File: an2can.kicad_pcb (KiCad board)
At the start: 2 copper layers, 76.7 x 51.9 mm, 130 parts, among them J1 PWR/CAN, J2 USB C, J3 DBG, J4 5V IN, J5 Input, J6 Aux, J7 Input, J8 Input, J9 Input, Q1 PMV65XP, SW1 RESET, U1 MAX6025, U10 AD8221ARZ, U11 Opamp_Dual, U12 AD8221ARZ, U13 Opamp_Dual, U2 Tex_DCDC_v2, U3 DSC61XX, U4 STM32L432KCUx, U5 MCP2562FD, U6 AD8221ARZ, U7 Opamp_Dual, U8 AD8221ARZ, U9 Opamp_Dual

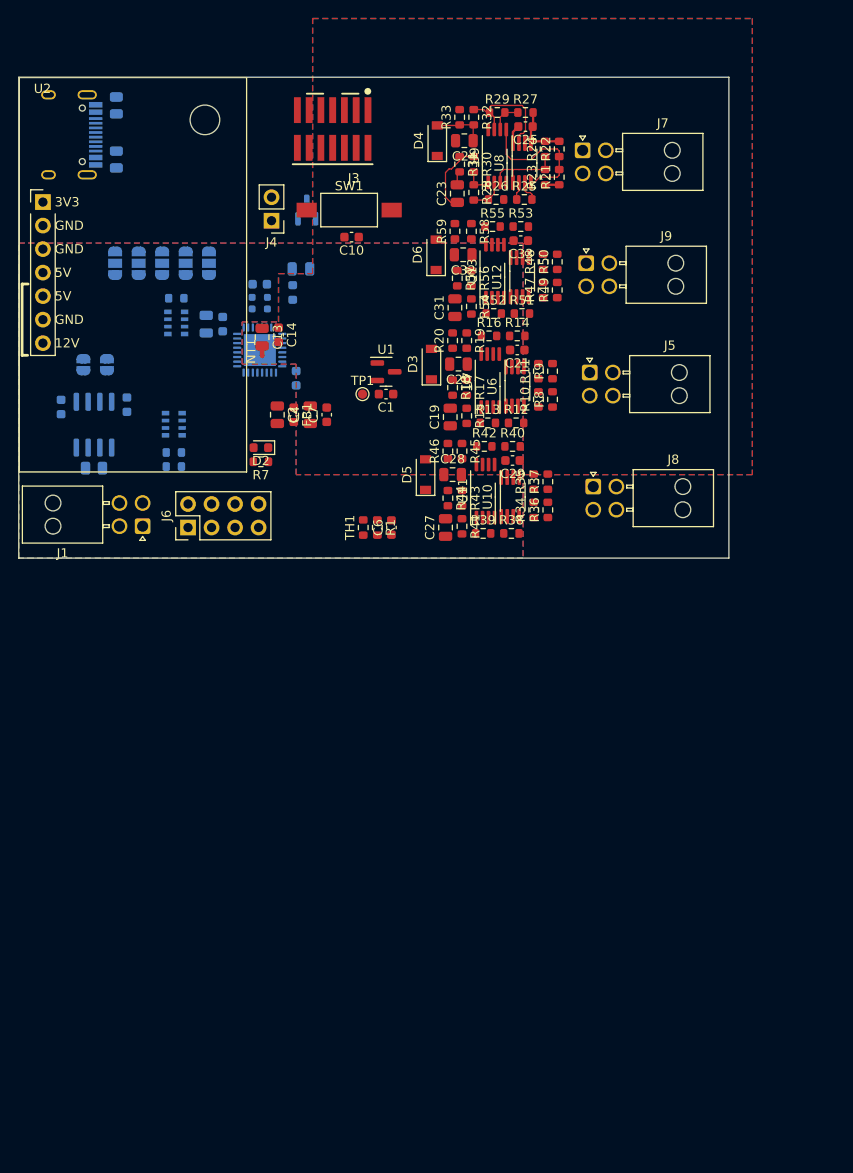
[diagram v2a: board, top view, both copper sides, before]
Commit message: pcb: define routing of input stage
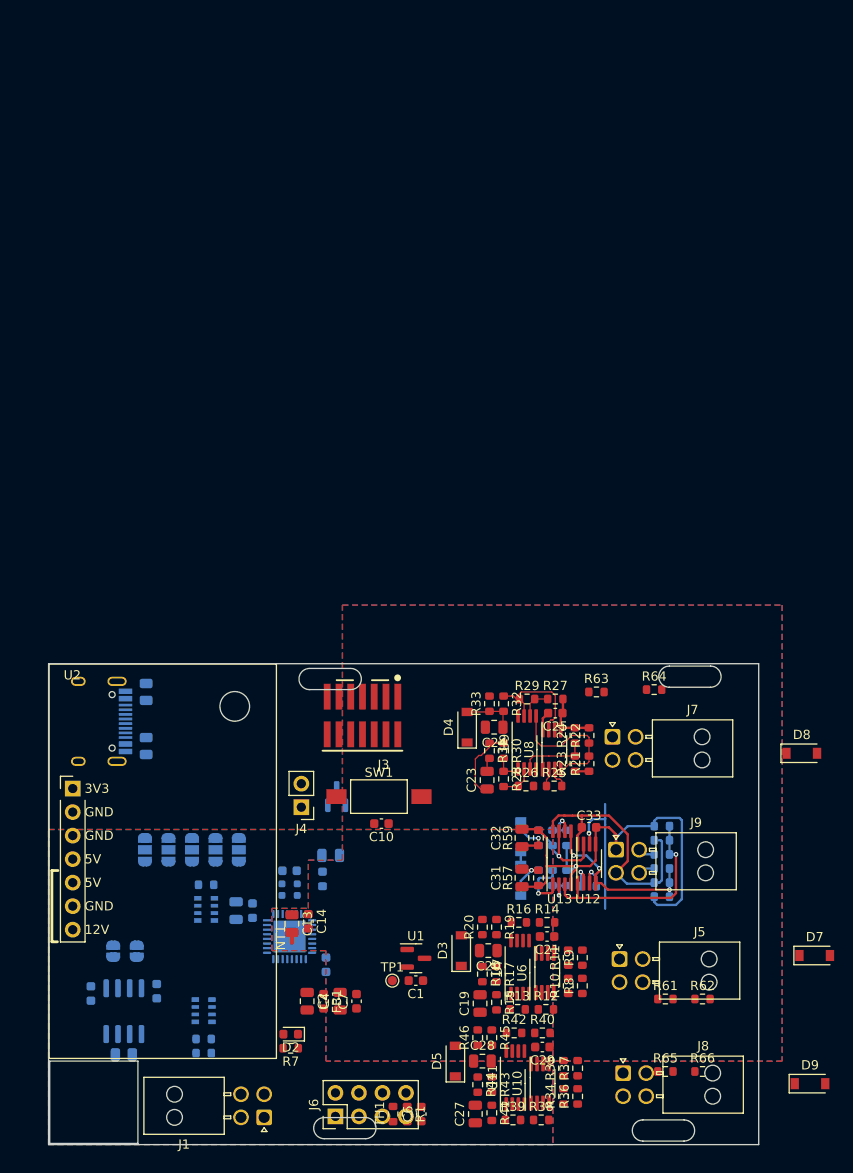
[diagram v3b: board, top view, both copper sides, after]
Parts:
- added D10: D_Schottky, Diode_SMD:D_SOD-123, B.Cu at (106.8, 88.3)
- added D7: D_Schottky, Diode_SMD:D_SOD-123, F.Cu at (138.6, 96.4)
- added D8: D_Schottky, Diode_SMD:D_SOD-123, F.Cu at (137.2, 74.5)
- added D9: D_Schottky, Diode_SMD:D_SOD-123, F.Cu at (138.0, 110.2)
- added R61: R, Resistor_SMD:R_0603_1608Metric, F.Cu at (122.4, 101.1)
- added R62: R, Resistor_SMD:R_0603_1608Metric, F.Cu at (126.4, 101.1)
- added R63: R, Resistor_SMD:R_0603_1608Metric, F.Cu at (115.0, 67.9)
- added R64: R, Resistor_SMD:R_0603_1608Metric, F.Cu at (121.2, 67.7)
- added R65: R, Resistor_SMD:R_0603_1608Metric, F.Cu at (122.4, 108.9)
- added R66: R, Resistor_SMD:R_0603_1608Metric, F.Cu at (126.4, 108.9)
- added R67: R, Resistor_SMD:R_0603_1608Metric, B.Cu at (122.0, 87.0)
- added R68: R, Resistor_SMD:R_0603_1608Metric, B.Cu at (122.0, 85.5)
- D6, R47, R48, R49, R50, R51, R52, R53, R54, R55, R56, R58: moved to B.Cu
- moved R48 69.8 mm to (122.0, 90.0), turned to 180 degrees
- moved R55 66.4 mm to (110.2, 83.7), turned to 90 degrees
- moved R53 66.2 mm to (111.8, 83.7), turned to -90 degrees
- moved R59 66.1 mm to (108.7, 83.7)
- moved R58 65.9 mm to (108.7, 83.7)
- moved J6 65.6 mm to (86.8, 113.8)
- moved R57 65.4 mm to (108.7, 88.0)
- moved R47 65.3 mm to (122.0, 88.5), turned to 0 degrees
- moved J1 65.2 mm to (79.1, 113.9)
- moved R56 65.2 mm to (108.7, 88.0)
- moved C33 63.8 mm to (114.2, 82.5)
- moved U12 63.8 mm to (113.9, 86.5)
- moved U13 63.8 mm to (111.3, 85.8)
- moved D6 63.5 mm to (106.8, 83.6)
- moved FB2 63.4 mm to (85.4, 88.1)
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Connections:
- J5 pad 1: /Input Stage 2/IN_0+ -> GNDA
- J5 pad 2: /Input Stage 2/IN_1+ -> +5VA
- J5 pad 3: +5VA -> /Input Stage 2/IN_1
- J5 pad 4: GNDA -> /Input Stage 2/IN_0
- J7 pad 1: /Input Stage 1/IN_0+ -> GNDA
- J7 pad 2: /Input Stage 1/IN_1+ -> +5VA
- J7 pad 3: +5VA -> /Input Stage 1/IN_1
- J7 pad 4: GNDA -> /Input Stage 1/IN_0
- J8 pad 1: /Input Stage 3/IN_0+ -> GNDA
- J8 pad 2: /Input Stage 3/IN_1+ -> +5VA
- J8 pad 3: +5VA -> /Input Stage 3/IN_1
- J8 pad 4: GNDA -> /Input Stage 3/IN_0
- J9 pad 1: /Input Stage 4/IN_0+ -> GNDA
- J9 pad 2: /Input Stage 4/IN_1+ -> +5VA
- J9 pad 3: +5VA -> /Input Stage 4/IN_1
- J9 pad 4: GNDA -> /Input Stage 4/IN_0
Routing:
- net GNDA: track 7.89 -> 60.0 mm, vias 0 -> 1
- net +5VA: track 3.59 -> 32.4 mm
- net /Input Stage 4/IN_1+: track 0.00 -> 23.0 mm, vias 0 -> 1
- net /Input Stage 4/IN_0+: track 0.00 -> 19.2 mm, vias 0 -> 3
- net /2V5_OFFSET: track 0.00 -> 15.6 mm, vias 0 -> 1
- net /Input Stage 4/OUT_COM_UNFLT: track 0.00 -> 10.8 mm, vias 0 -> 1
- net /Input Stage 4/OUT_COM: track 0.00 -> 6.60 mm, vias 0 -> 1
- net /Input Stage 4/OUT_SINGLE_UNFLT: track 0.00 -> 6.32 mm, vias 0 -> 1
- net /Input Stage 4/OUT_SINGLE: track 0.00 -> 5.79 mm, vias 0 -> 1
- net /Input Stage 4/IN_1-: track 0.00 -> 4.43 mm, vias 0 -> 1
- net /Input Stage 4/IN_0-: track 0.00 -> 3.84 mm, vias 0 -> 1
- net /Input Stage 4/RG2: track 0.00 -> 3.04 mm, vias 0 -> 1
- net /Input Stage 4/RG1: track 0.00 -> 2.88 mm, vias 0 -> 1
- net /Input Stage 4/IN_1: track 0.00 -> 1.84 mm
- net /Input Stage 4/IN_0: track 0.00 -> 1.82 mm
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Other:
- outline, holes or cut-outs redrawn

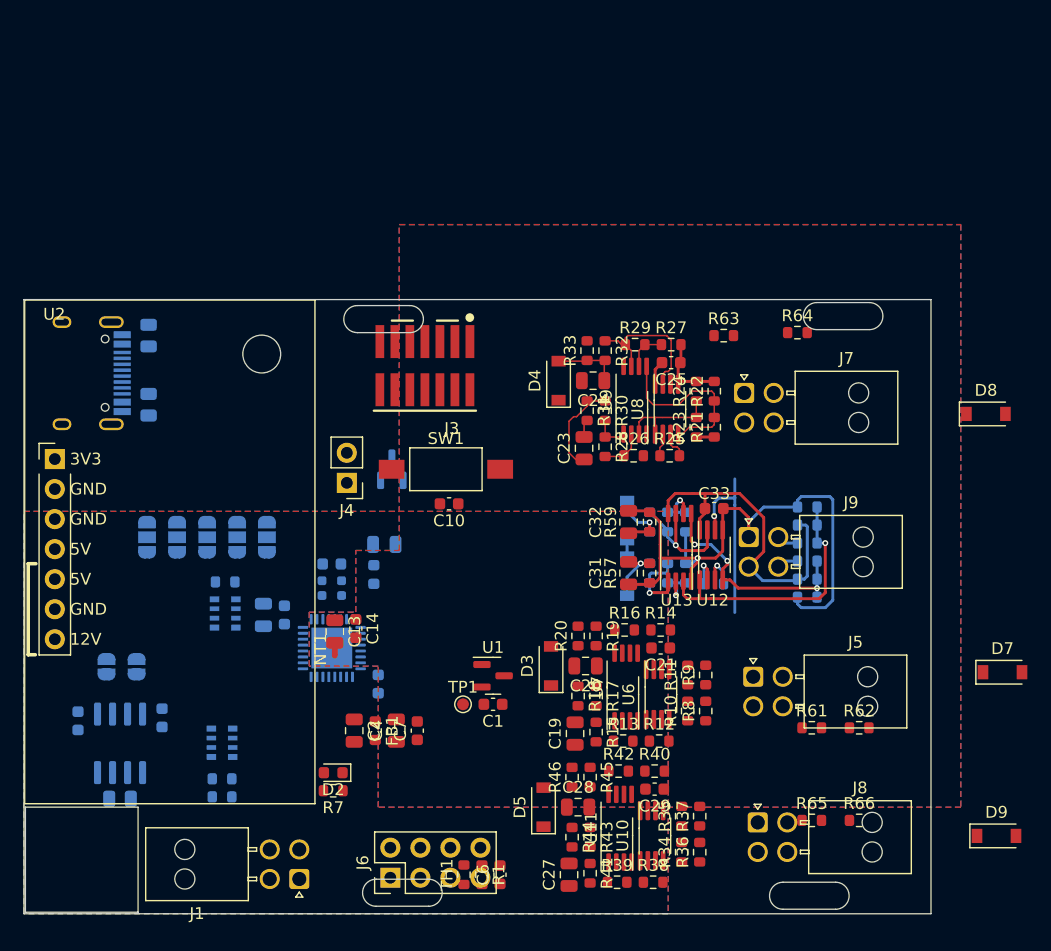
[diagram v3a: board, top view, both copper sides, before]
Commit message: pcb: finalize routing of analog section
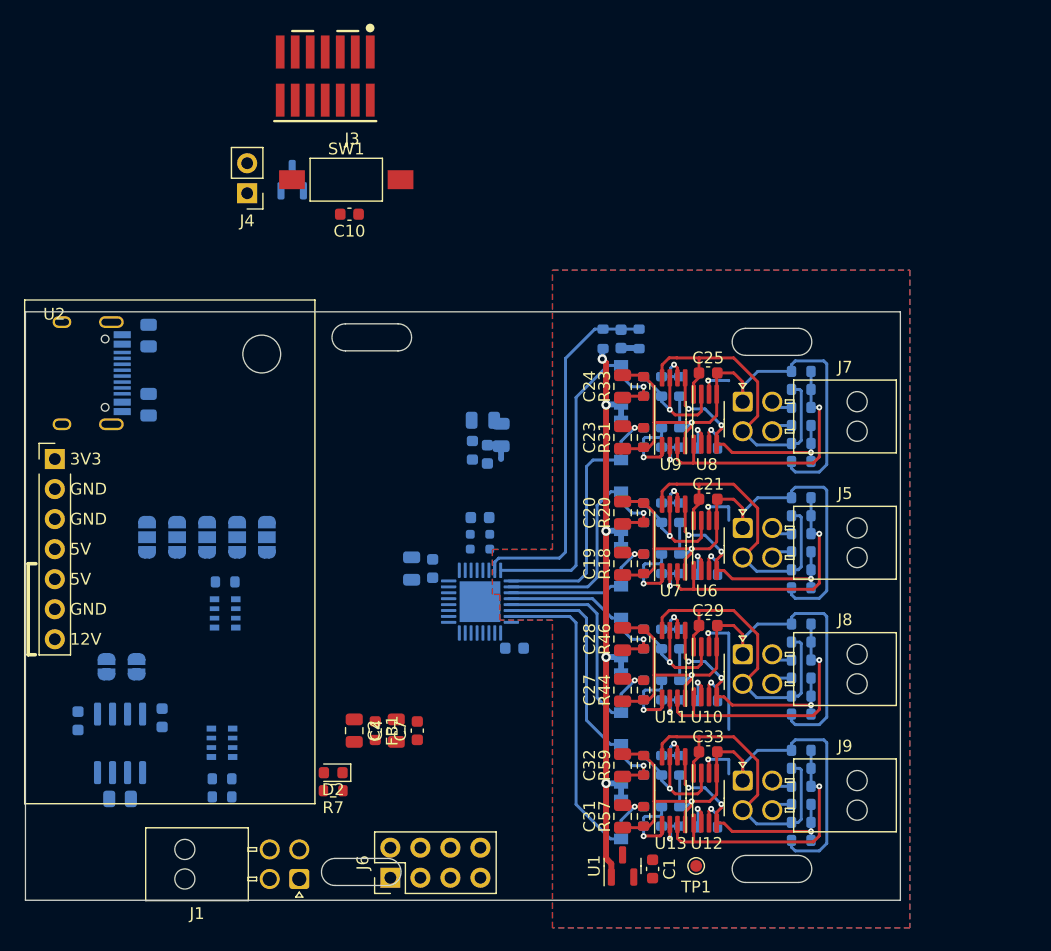
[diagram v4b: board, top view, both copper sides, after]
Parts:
- C13, C14, C6, D3, D4, D5, D7, D8, D9, NT1, R1, R10, R11, R12, R13, R14, R15, R16, R17, R19, R21, R22, R23, R24, R25, R26, R27, R28, R29, R30, R32, R34, R35, R36, R37, R38, R39, R40, R41, R42, R43, R45, R61, R62, R63, R64, R65, R66, R8, R9, TH1: moved to B.Cu
- moved R1 47.2 mm to (107.8, 68.2)
- moved TH1 46.8 mm to (104.8, 68.2)
- moved C6 46.5 mm to (106.3, 68.2)
- moved D9 34.0 mm to (106.3, 98.2), turned to -90 degrees
- moved D7 33.5 mm to (106.3, 87.5), turned to -90 degrees
- moved D8 30.9 mm to (106.3, 76.8), turned to -90 degrees
- moved C10 25.9 mm to (83.3, 57.7)
- moved J3 25.9 mm to (81.3, 46.0)
- moved J4 25.9 mm to (74.7, 55.9)
- moved Q1 25.9 mm to (78.5, 54.7)
- moved SW1 25.9 mm to (83.1, 54.7)
- moved TP1 24.0 mm to (112.6, 112.8)
- moved C13 21.8 mm to (96.2, 76.3)
- moved NT1 21.8 mm to (96.2, 77.9)
- moved J9 20.6 mm to (116.6, 105.6)
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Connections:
- U4 pad 10: /Input Stage 2/OUT_SINGLE -> /Input Stage 2/OUT_COM
- U4 pad 11: /Input Stage 2/OUT_COM -> /Input Stage 2/OUT_SINGLE
- U4 pad 12: /Input Stage 3/OUT_SINGLE -> /Input Stage 3/OUT_COM
- U4 pad 13: /Input Stage 3/OUT_COM -> /Input Stage 3/OUT_SINGLE
- U4 pad 14: /Input Stage 4/OUT_SINGLE -> /Input Stage 4/OUT_COM
- U4 pad 15: /Input Stage 4/OUT_COM -> /Input Stage 4/OUT_SINGLE
- U4 pad 8: /Input Stage 1/OUT_SINGLE -> /Input Stage 1/OUT_COM
- U4 pad 9: /Input Stage 1/OUT_COM -> /Input Stage 1/OUT_SINGLE
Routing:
- net GNDA: track 60.0 -> 208.1 mm, vias 1 -> 4
- net +5VA: track 32.4 -> 115.4 mm
- net +3.3VA: track 1.40 -> 55.7 mm, vias 0 -> 5
- net /Temp: track 0.00 -> 30.8 mm
- net /Input Stage 1/OUT_COM: track 5.71 -> 32.1 mm, vias 0 -> 1
- net /Input Stage 4/OUT_SINGLE: track 5.79 -> 31.9 mm
- net /Input Stage 3/OUT_SINGLE: track 0.00 -> 23.0 mm, vias 0 -> 1
- net /Input Stage 2/IN_1+: track 0.00 -> 23.0 mm, vias 0 -> 1
- net /Input Stage 3/IN_1+: track 0.00 -> 23.0 mm, vias 0 -> 1
- net /Input Stage 2/OUT_COM: track 0.00 -> 22.8 mm, vias 0 -> 1
- net /Input Stage 3/IN_0+: track 0.00 -> 19.2 mm, vias 0 -> 3
- net /Input Stage 2/IN_0+: track 0.00 -> 19.2 mm, vias 0 -> 3
- net /Input Stage 4/OUT_COM: track 6.60 -> 25.7 mm
- net /Input Stage 3/OUT_COM: track 0.00 -> 16.6 mm, vias 0 -> 1
- net /Input Stage 1/OUT_SINGLE: track 8.19 -> 24.6 mm, vias 0 -> 1
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- removed copper zone on B.Cu, net GND
- removed copper zone on F.Cu, net GND
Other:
- board size 76.7 x 51.9 mm -> 74 x 49.8 mm

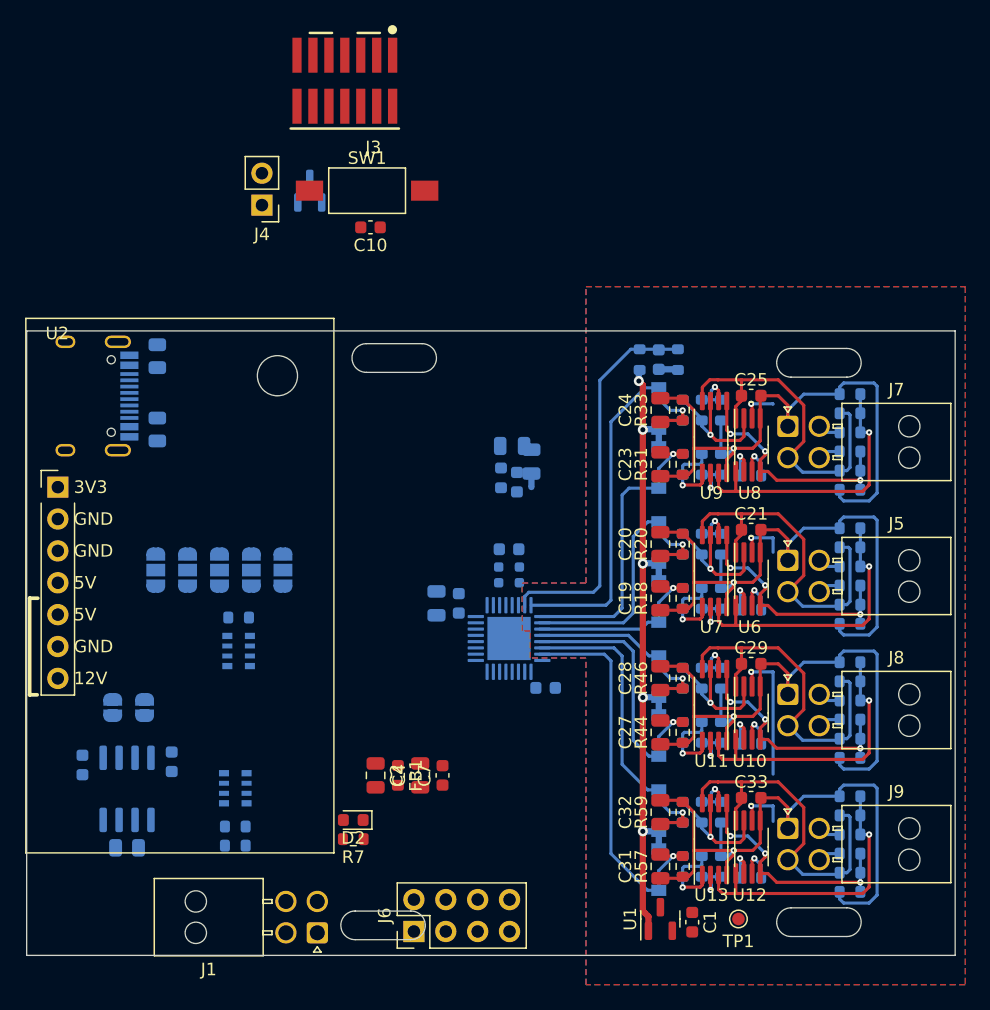
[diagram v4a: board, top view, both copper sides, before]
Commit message: pcb: continue routing of digital section
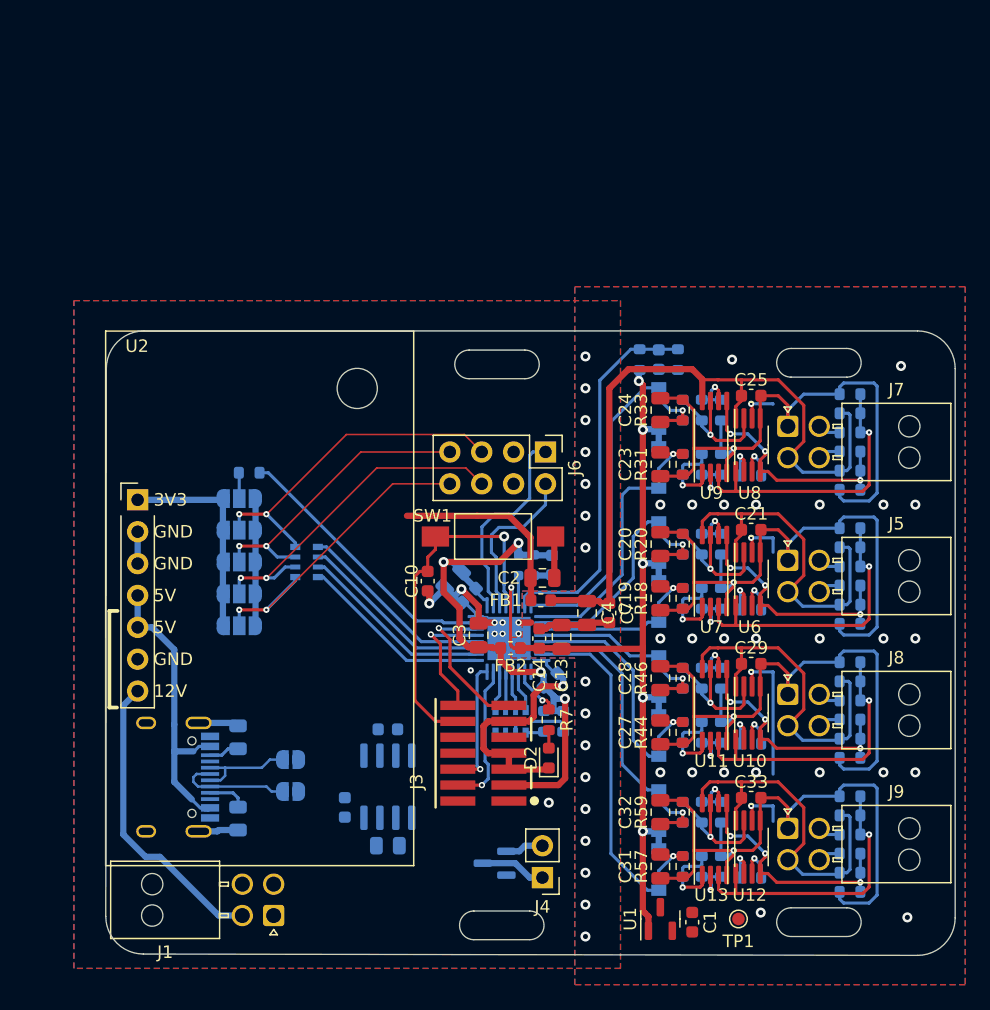
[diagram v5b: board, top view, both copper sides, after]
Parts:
- C13, C14, C3, FB2, NT1: moved to F.Cu
- moved J4 58.1 mm to (97.0, 109.5)
- moved Q1 55.6 mm to (93.2, 108.3), turned to 180 degrees
- moved J3 54.7 mm to (92.3, 99.6), turned to 90 degrees
- moved J6 39.6 mm to (97.3, 75.6), turned to -90 degrees
- moved R3 31.7 mm to (72.8, 104.8)
- moved J2 31.0 mm to (66.5, 101.5)
- moved R2 31.0 mm to (72.8, 98.3)
- moved SW1 29.3 mm to (93.1, 82.3), turned to 180 degrees
- moved C10 28.6 mm to (87.9, 85.9), turned to -90 degrees
- moved R5 27.4 mm to (98.7, 97.0), turned to -90 degrees
- moved R4 26.5 mm to (97.2, 97.0), turned to -90 degrees
- moved RN2 22.6 mm to (94.5, 97.0), turned to 90 degrees
- moved C16 21.2 mm to (81.3, 103.9)
- moved R6 20.8 mm to (84.7, 106.9)
- moved U5 20.8 mm to (84.7, 102.2)
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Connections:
- J6 pad 1: /MCU/I2C_SCL -> /MCU/Spare1
- J6 pad 2: /A0 -> /MCU/Spare2
- J6 pad 3: /MCU/I2C_SDA -> /MCU/I2C_SCL
- J6 pad 4: /A1 -> /MCU/I2C_SDA
- J6 pad 5: /MCU/Spare1 -> /A3
- J6 pad 6: /A2 -> /A1
- J6 pad 7: /MCU/Spare2 -> /A2
- J6 pad 8: /A3 -> /A0
- RN1 pad 5: /A3 -> /A0
- RN1 pad 6: /A0 -> /A1
- RN1 pad 7: /A1 -> /A2
- RN1 pad 8: /A2 -> /A3
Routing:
- net GND: track 0.00 -> 65.5 mm, vias 0 -> 11
- net +3V3: track 0.00 -> 64.7 mm, vias 0 -> 4
- net +5V: track 0.00 -> 39.6 mm
- net +5VA: track 115.4 -> 147.7 mm
- net /MCU/~{RESET}: track 0.00 -> 29.2 mm, vias 0 -> 1
- net /A3: track 0.00 -> 27.4 mm, vias 0 -> 2
- net /A1: track 0.00 -> 27.3 mm, vias 0 -> 2
- net /A0: track 0.00 -> 25.8 mm, vias 0 -> 2
- net VDC: track 0.00 -> 24.1 mm
- net /A2: track 0.00 -> 23.8 mm, vias 0 -> 2
- net /MCU/BOOT0: track 0.00 -> 22.2 mm
- net +3.3VA: track 55.7 -> 72.4 mm, vias 5 -> 6
- net /MCU/Spare1: track 0.00 -> 16.2 mm
- net Net-(RN1-Pad1): track 0.00 -> 15.7 mm
- net Net-(RN1-Pad2): track 0.00 -> 15.6 mm
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- added copper zone on B.Cu, net GND
- added copper zone on F.Cu, net GND
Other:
- board size 74 x 49.8 mm -> 67.7 x 49.8 mm
